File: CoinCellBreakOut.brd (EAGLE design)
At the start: 34 x 20 mm, 6 parts, among them U1 LP3985IM5-3.0

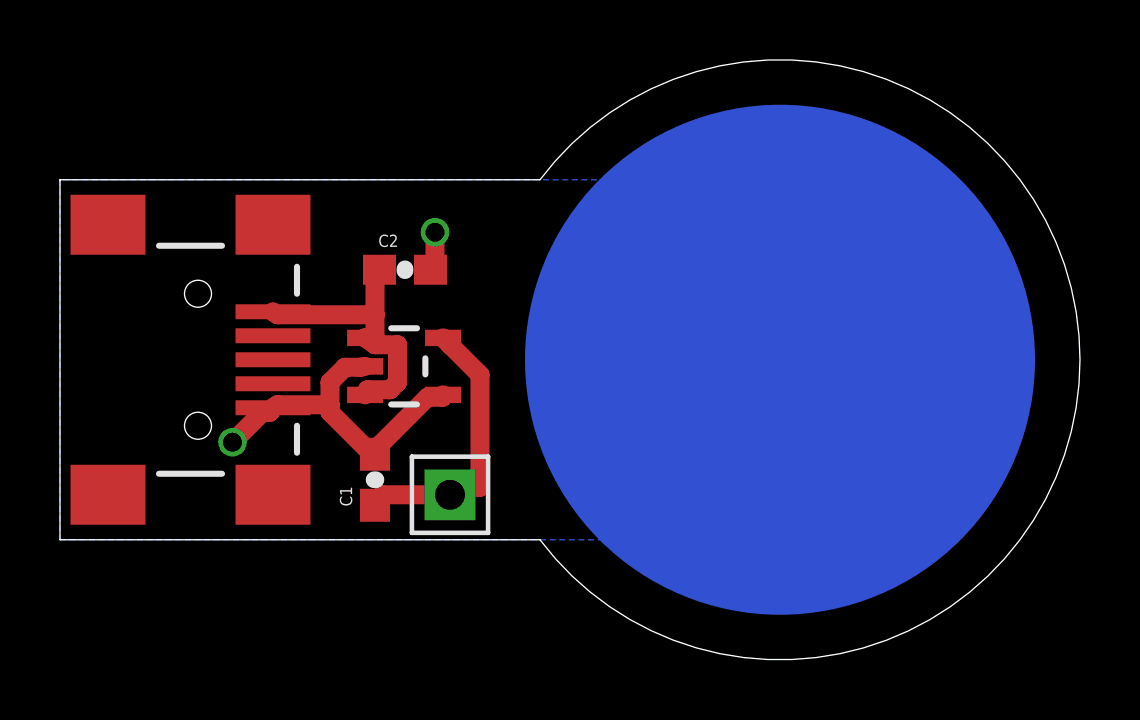
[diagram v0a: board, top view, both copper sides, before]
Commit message: fixed tracks near usb connector
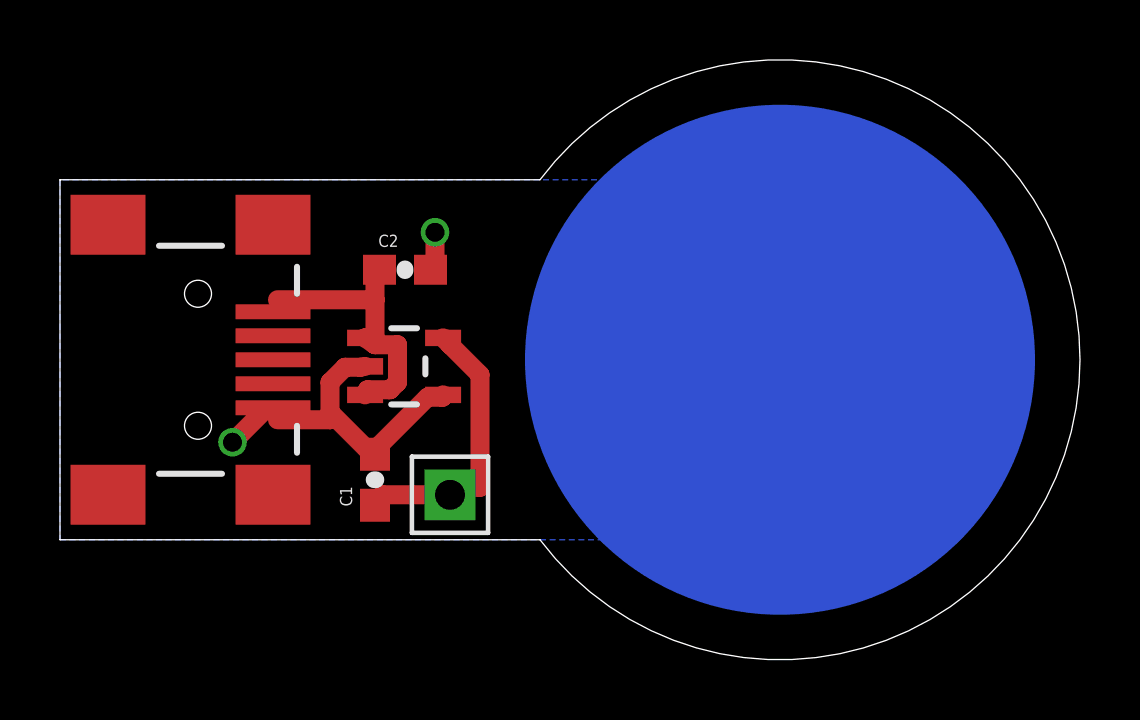
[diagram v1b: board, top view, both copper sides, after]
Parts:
- C1, C2: value (none) -> 1u
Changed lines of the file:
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@@
 <?xml version="1.0" encoding="utf-8"?>
 <!DOCTYPE eagle SYSTEM "eagle.dtd">
-<eagle version="7.2.0">
+<eagle version="7.7.0">
 <drawing>
 <settings>
@@
 </element>
 <element name="3V" library="dp_devices" package="M1X2_10_17" value="CON_HEADER_1X01-PTH_10_17" x="13" y="5.5" smashed="yes"/>
-<element name="C1" library="SparkFun-Capacitors" package="0603-CAP" value="" x="10.5" y="6" rot="R90"/>
-<element name="C2" library="SparkFun-Capacitors" package="0603-CAP" value="" x="11.5" y="13"/>
+<element name="C1" library="SparkFun-Capacitors" package="0603-CAP" value="1u" x="10.5" y="6" rot="R90"/>
+<element name="C2" library="SparkFun-Capacitors" package="0603-CAP" value="1u" x="11.5" y="13"/>
 </elements>
 <signals>
@@
 <contactref element="JP1" pad="VBUS"/>
 <contactref element="C2" pad="1"/>
-<wire x1="10.5" y1="10.75" x2="10.5" y2="11.5" width="0.635" layer="1"/>
-<wire x1="10.5" y1="11.5" x2="10.5" y2="13" width="0.635" layer="1"/>
+<wire x1="10.5" y1="10.75" x2="10.5" y2="12" width="0.635" layer="1"/>
+<wire x1="10.5" y1="12" x2="10.5" y2="13" width="0.635" layer="1"/>
 <wire x1="10.25" y1="10.75" x2="10.5" y2="10.75" width="0.635" layer="1"/>
 <wire x1="10.5" y1="13" x2="10.65" y2="13" width="0.635" layer="1"/>
@@
 <wire x1="10.25" y1="9" x2="10.1699" y2="8.83" width="0.635" layer="1"/>
 <wire x1="10.5" y1="10.5" x2="10.1699" y2="10.73" width="0.635" layer="1"/>
-<wire x1="10.5" y1="11.5" x2="7.25" y2="11.5" width="0.635" layer="1"/>
-<wire x1="7.25" y1="11.5" x2="7.1" y2="11.6" width="0.635" layer="1"/>
+<wire x1="10.5" y1="12" x2="7.25" y2="12" width="0.635" layer="1"/>
+<wire x1="7.25" y1="12" x2="7.1" y2="11.6" width="0.3048" layer="1"/>
 </signal>
 <signal name="GND" class="1">
@@
 <wire x1="9.5" y1="9.75" x2="10" y2="9.75" width="0.635" layer="1"/>
 <wire x1="9" y1="9.25" x2="9.5" y2="9.75" width="0.635" layer="1"/>
-<wire x1="9" y1="8.5" x2="9" y2="9.25" width="0.635" layer="1"/>
-<wire x1="7.25" y1="8.5" x2="9" y2="8.5" width="0.635" layer="1"/>
+<wire x1="9" y1="8.25" x2="9" y2="9.25" width="0.635" layer="1"/>
+<wire x1="7.25" y1="8" x2="9" y2="8" width="0.635" layer="1"/>
 <wire x1="10" y1="9.75" x2="10.1699" y2="9.78" width="0.635" layer="1"/>
-<wire x1="7.25" y1="8.5" x2="7.1" y2="8.4" width="0.635" layer="1"/>
+<wire x1="7.25" y1="8" x2="7.1" y2="8.4" width="0.3048" layer="1"/>
 <wire x1="6.75" y1="8.25" x2="5.75" y2="7.25" width="0.635" layer="1"/>
-<wire x1="7" y1="8.25" x2="6.75" y2="8.25" width="0.635" layer="1"/>
-<wire x1="7" y1="8.25" x2="7.1" y2="8.4" width="0.635" layer="1"/>
+<wire x1="7" y1="8.25" x2="6.75" y2="8.25" width="0.3048" layer="1"/>
+<wire x1="7" y1="8.25" x2="7.1" y2="8.4" width="0.3048" layer="1"/>
 <wire x1="9" y1="8.25" x2="10.25" y2="7" width="0.635" layer="1"/>
 <wire x1="10.25" y1="7" x2="10.5" y2="6.85" width="0.635" layer="1"/>
-<wire x1="9" y1="8.25" x2="9" y2="8.5" width="0.635" layer="1"/>
+<wire x1="9" y1="8.25" x2="9" y2="8" width="0.635" layer="1"/>
 <via x="12.5" y="14.25" extent="1-16" drill="0.635"/>
 <via x="5.75" y="7.25" extent="1-16" drill="0.635"/>
